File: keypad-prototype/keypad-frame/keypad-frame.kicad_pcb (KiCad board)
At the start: 2 copper layers, 150.2 x 64.2 mm, 13 parts, among them SW2 Switch_SW_Push, SW3 Switch_SW_Push, SW4 Switch_SW_Push, SW5 Switch_SW_Push, SW6 Switch_SW_Push, SW7 Switch_SW_Push, U3 IE096HQ1301CL_SLOT, U4 IE096HQ1301CL_SLOT, U5 IE096HQ1301CL_SLOT, U6 IE096HQ1301CL_SLOT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

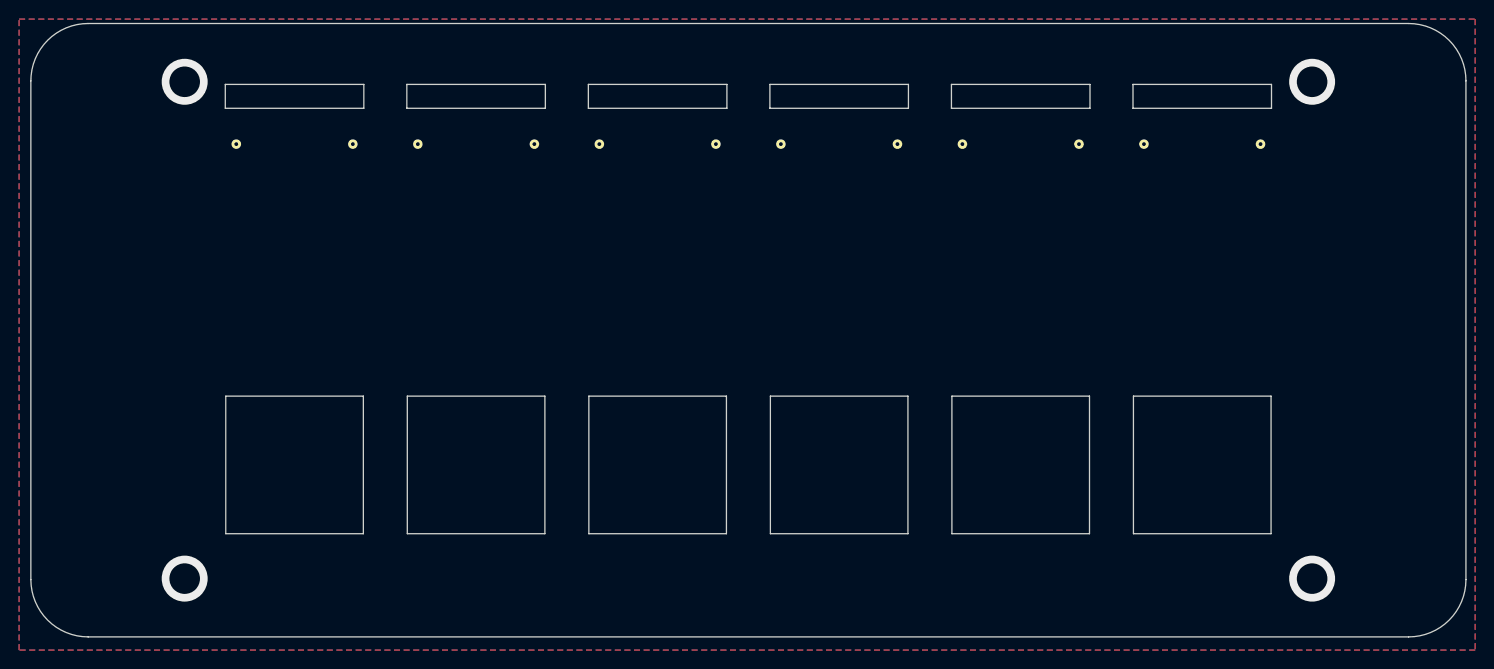
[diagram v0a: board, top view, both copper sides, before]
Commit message: keypad-base/keypad-frame: change to M2 standoffs, Apr2021a release
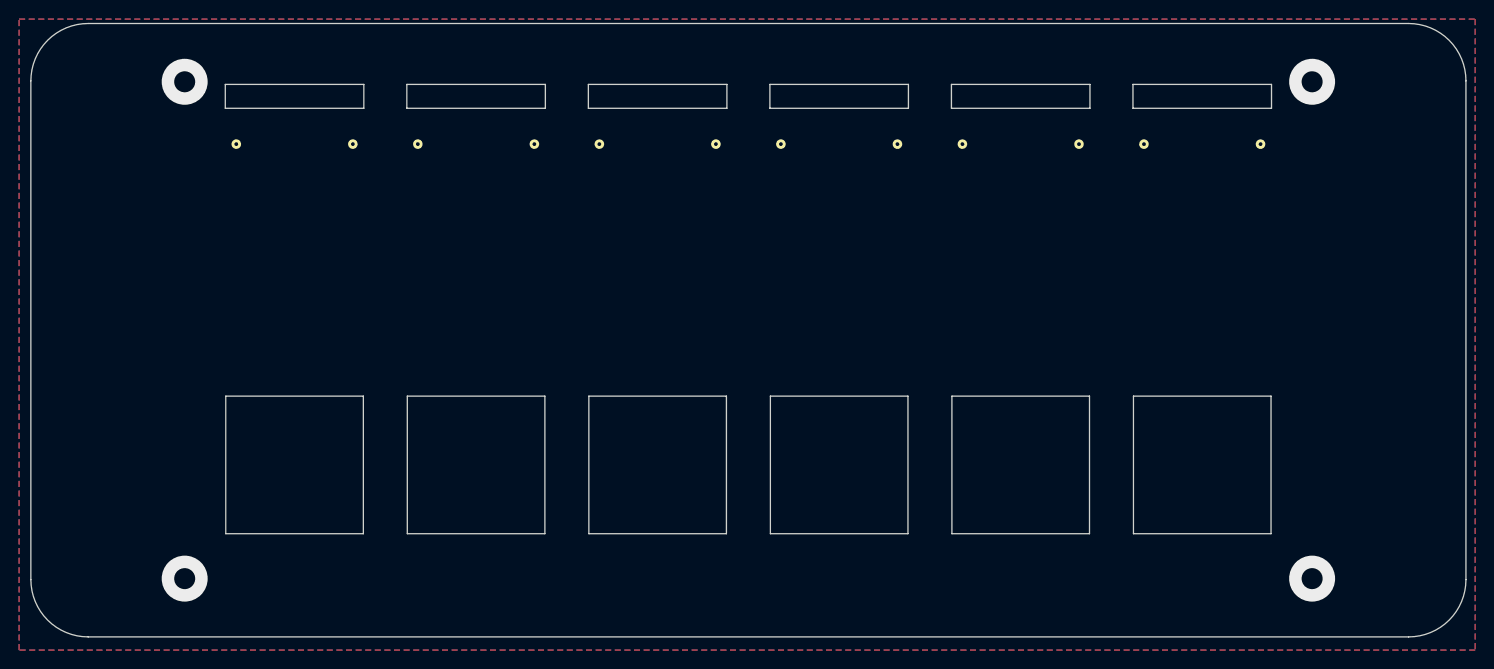
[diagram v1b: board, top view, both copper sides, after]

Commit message: keypad-frame: May2021 release, change to m3 holes, shrink keyswitch cutouts
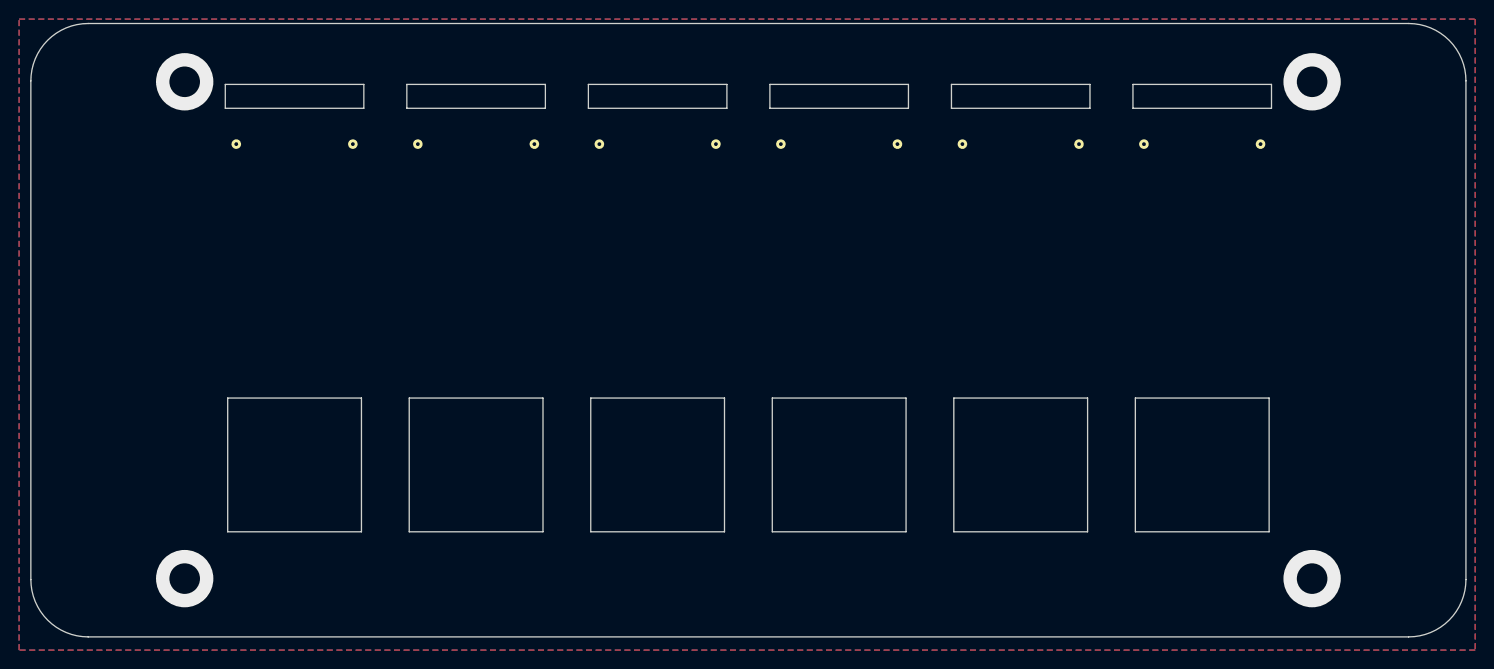
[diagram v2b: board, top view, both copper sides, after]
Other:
- board text added: "keypad-frame @TomKeddie May2021"
- board text removed: "keypad-frame @TomKeddie Apr2021"
